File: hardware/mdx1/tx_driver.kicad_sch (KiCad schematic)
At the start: 46 parts, among them Q4 BSC320N20NS3 G, Q5 BSC320N20NS3 G, Q6 BSC320N20NS3 G, Q7 BSC320N20NS3 G, U10 UCC27714D, U11 UCC27714D, U12 INA241A2 (20 V/V), U13 TLV3501 4.5 V (+5 A), U14 TLV3501 0.5 V (-5 A)

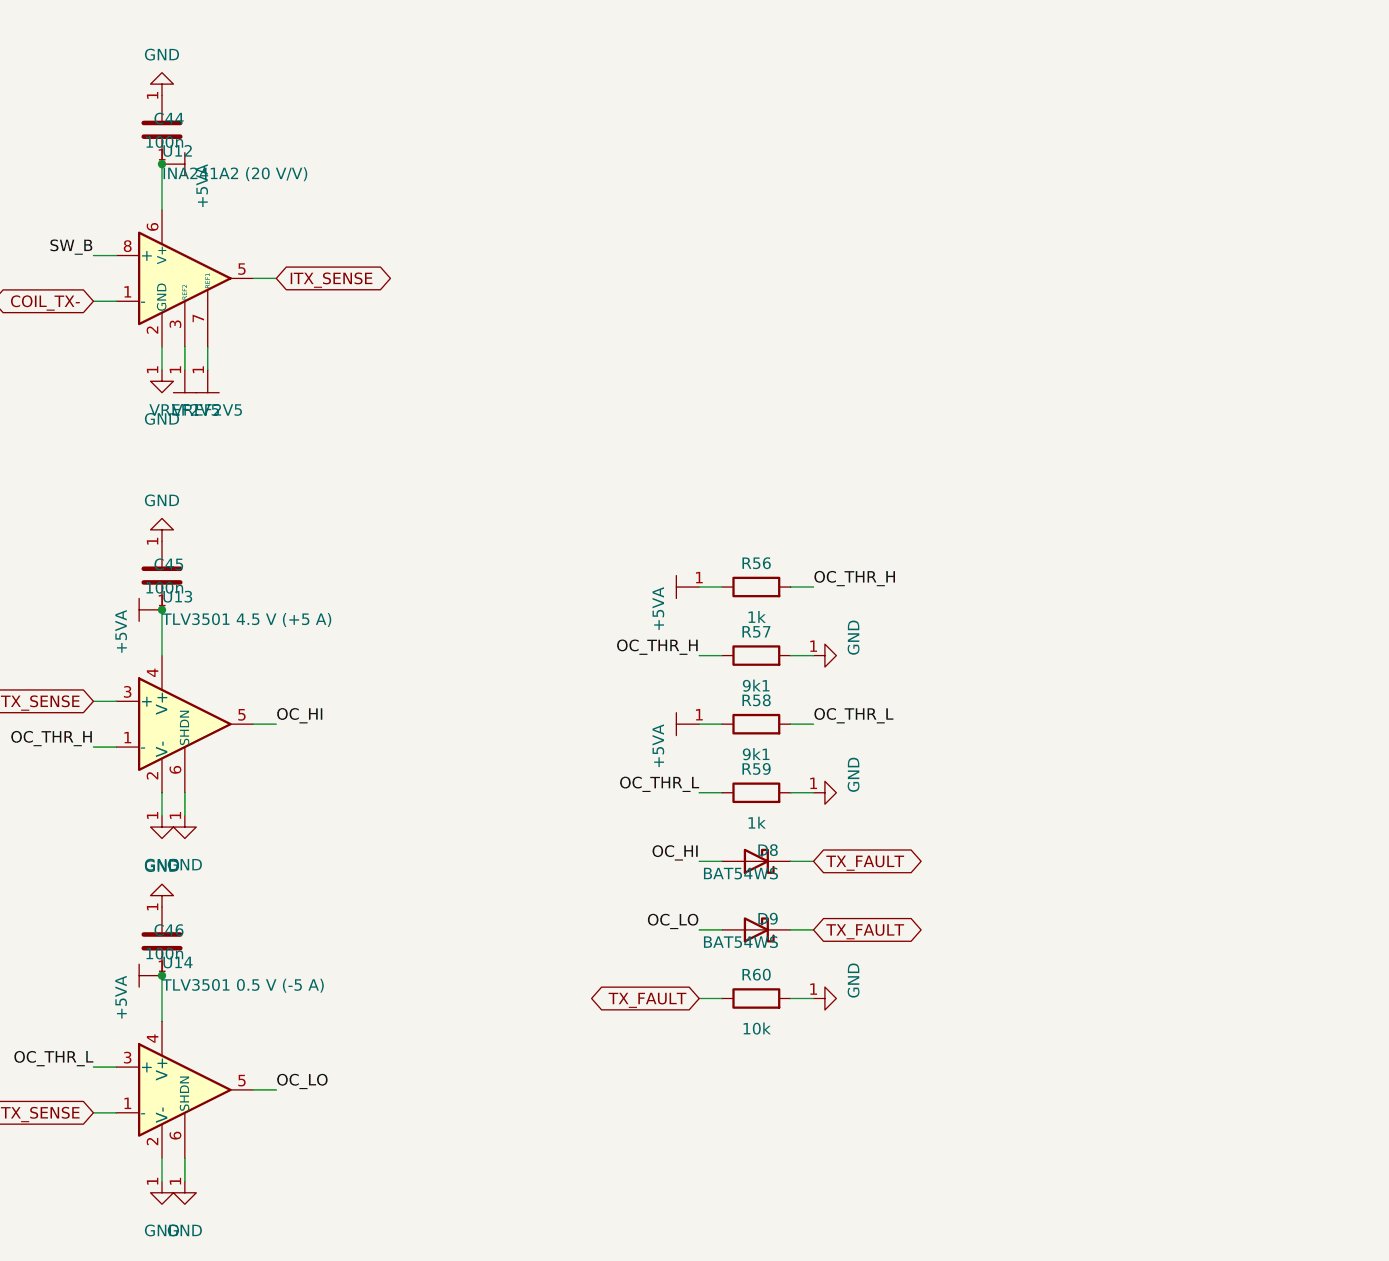
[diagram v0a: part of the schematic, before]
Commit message: Re-source out-of-stock parts; rework D8/9 footprint and GNSS antenna front end
Parts re-sourced to in-stock equivalents (BOM + board + firmware kept in sync):
- U4  TPS65131RGET, U12 INA241A2QDGKRQ1, U23 LSM6DSO32TR (same footprints)
- Q1  SiR680ADP-T1-UE3 (80 V, same PowerPAK SO-8; higher Qg - verify gate drive)
- U2  BQ27441DRZT-G1A (drop-in, R9 sense retained)
- D8/9 NSVBAT54SWT1G: SOT-323/SC-70 dual-series wired as a single diode
  (anode=pin1, cathode=pin3, pin2 NC); footprint changed on the board
- C32/C33/C38-48 re-sourced (KEMET/Murata/TDK), same footprints

GNSS antenna: chip antenna -> external active antenna via u.FL
- Removed U28 (chip antenna), C115 (match pad), R111 (0R RF series-match)
- Added J13 u.FL (Molex 73412-0110) + bias-tee: L8 27nH feed, C127 33pF DC block,
  C128 10nF VCC_RF bypass, D17 PESD0402-140 ESD (verify Vrwm >= 5 V)

Firmware:
- mdx_config.h: MDX_ITX_V_PER_A 0.4 -> 1.0 (INA241A2 is 50 V/V, not 20)
- hal_stm32.c: LSM6DSO32 accel init 0x48 -> 0x40 (FS_XL encoding differs; keeps +-4 g)
- make test: 96 checks pass

BOM: bom_data.json reconciled to the updated board (every placed part has an MPN;
fab BOM drops only the 15 test points). Regenerated JLCPCB fab package and the
DigiKey upload BOM (grouped by MPN, compact references).
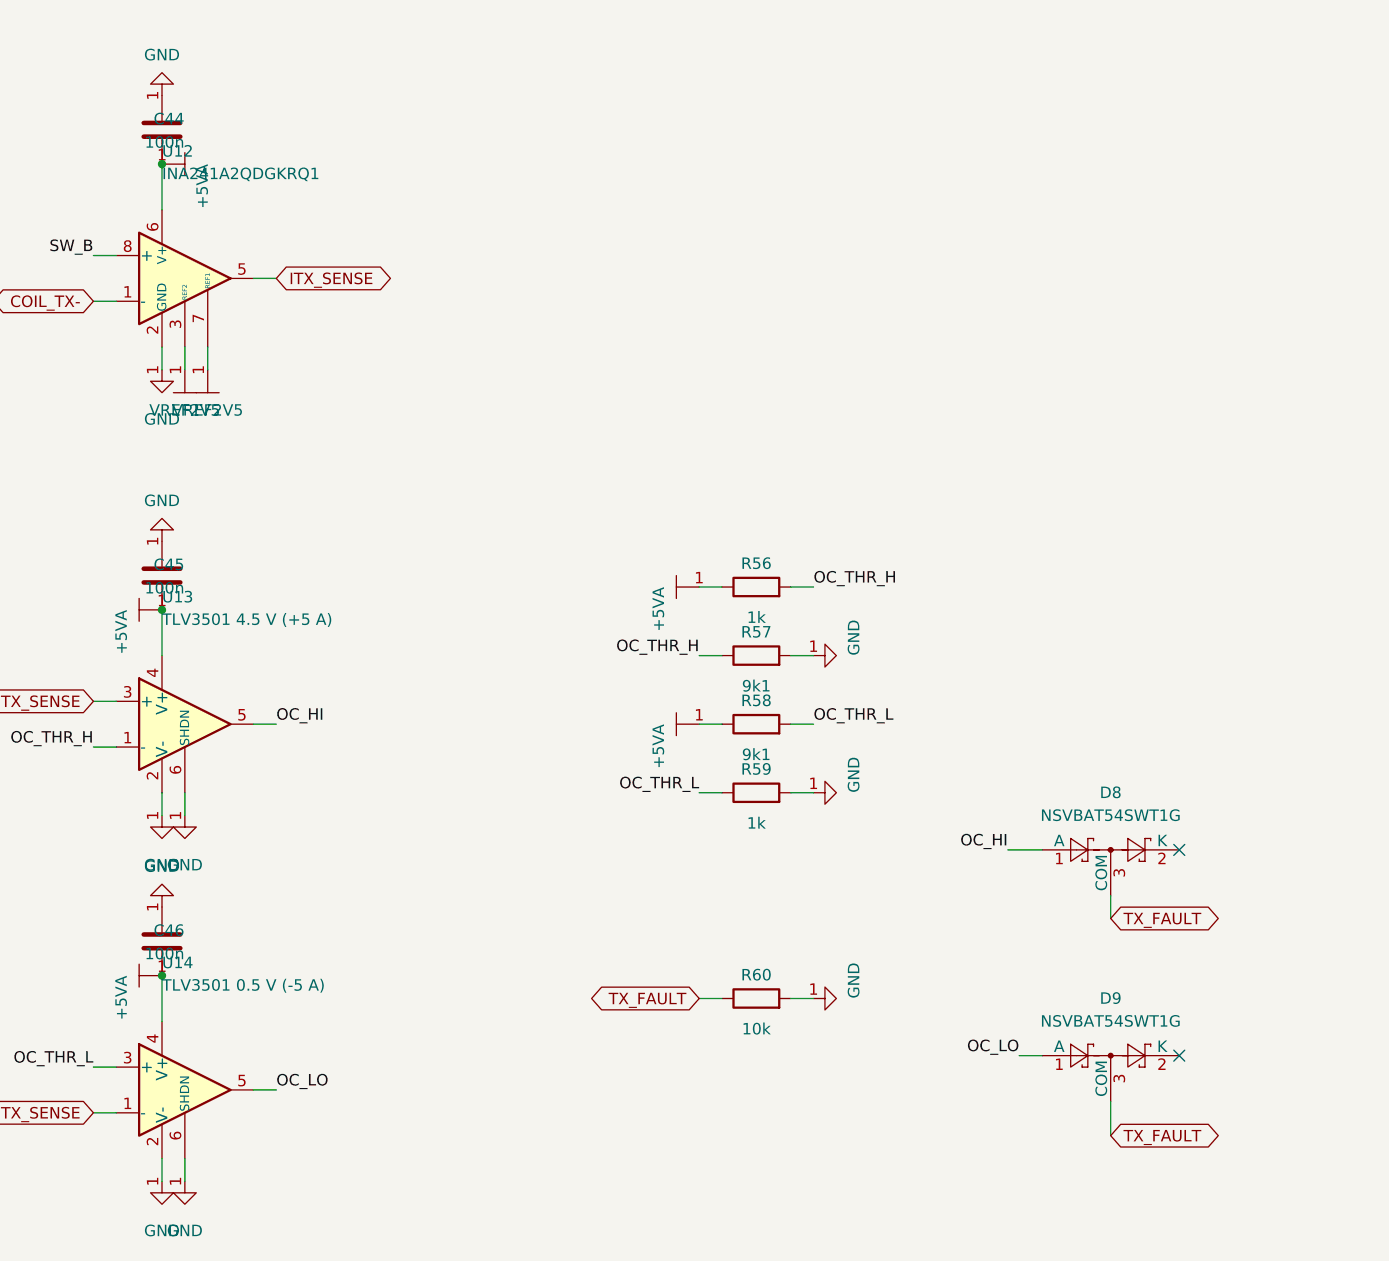
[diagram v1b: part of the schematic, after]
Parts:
- removed D8, D9: BAT54WS, Diode_SMD:D_SOD-323, symbol Device:D_Schottky
- added D8, D9: NSVBAT54SWT1G, Package_TO_SOT_SMD:SOT-323_SC-70, symbol Diode:BAT54SW
- U12: value INA241A2 (20 V/V) -> INA241A2QDGKRQ1
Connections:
- net OC_HI: now also D8.1 (A)
- net OC_LO: now also D9.1 (A)
- net TX_FAULT: now also D8.3 (COM), D9.3 (COM)
- no-connect marks 8 -> 10
